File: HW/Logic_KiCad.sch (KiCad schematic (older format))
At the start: 11 parts, among them SW1 SW_SPDT, U1 ESP32-PICO-D4

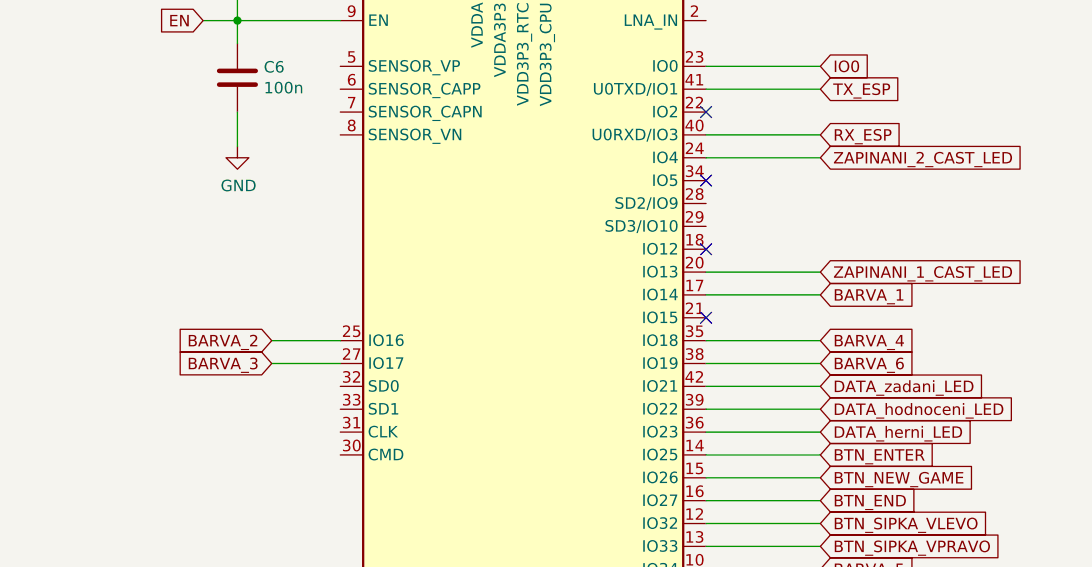
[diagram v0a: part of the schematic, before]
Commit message: repair mistake with tranzistors, repair programming ESP PICO
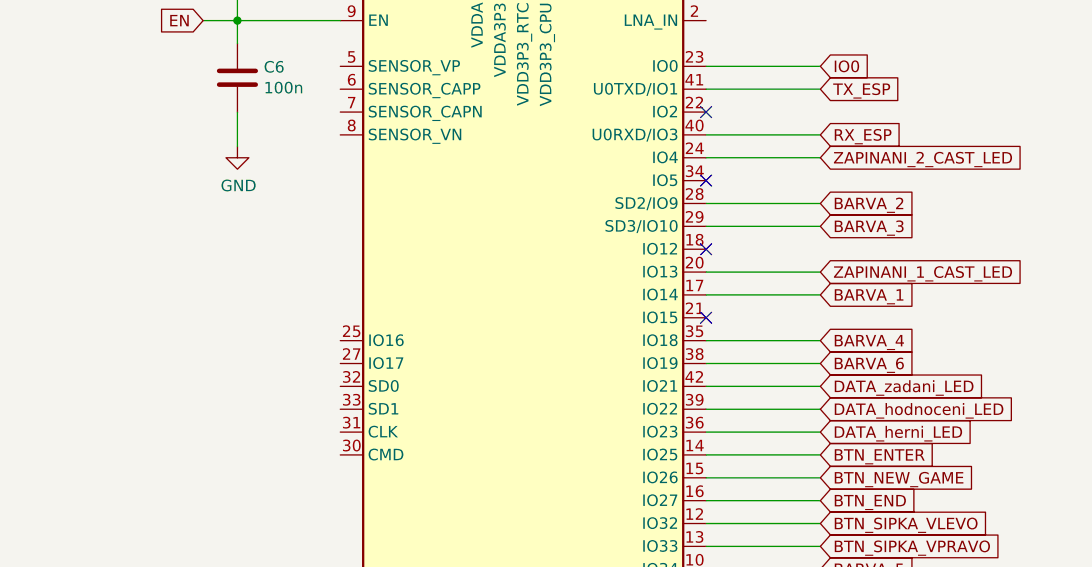
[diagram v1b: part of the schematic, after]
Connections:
- net BARVA_2: now also U1.28 (SD2/IO9); no longer U1.25 (IO16)
- net BARVA_3: now also U1.29 (SD3/IO10); no longer U1.27 (IO17)
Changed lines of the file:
@@
 Text GLabel 5950 5450 2    50   Input ~ 0
 BARVA_1
-Text GLabel 3550 5650 0    50   Input ~ 0
+Text GLabel 5950 5050 2    50   Input ~ 0
 BARVA_2
 Wire Wire Line
@@
 F6 "GPIO_2" I R 1600 7150 50
 $EndSheet
-Text GLabel 3550 5750 0    50   Input ~ 0
+Text GLabel 5950 5150 2    50   Input ~ 0
 BARVA_3
 Text GLabel 5950 5650 2    50   Input ~ 0
@@
 Text GLabel 5950 5750 2    50   Input ~ 0
 BARVA_6
-Wire Wire Line
-	3550 5650 3850 5650
-Wire Wire Line
-	3850 5750 3550 5750
 Text GLabel 9750 4450 0    50   Input ~ 0
 BARVA_5
@@
 Wire Wire Line
 	9750 4050 9950 4050
+Wire Wire Line
+	5950 5050 5450 5050
+Wire Wire Line
+	5450 5150 5950 5150
 $EndSCHEMATC

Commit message: deposit of DPS, start v1.0
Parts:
- added D?: green, LED_SMD:LED_0603_1608Metric, symbol Device:LED
- added H? (x4): MountingHole, symbol Mechanical:MountingHole
- added R? (x2): 10k, Resistor_SMD:R_0402_1005Metric, symbol Device:R
- C6: value 100n -> 1u; LCSC C1525 -> (none)
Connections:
- net +3V3: now also D?.2 (A), R?.2
- net BARVA_5: now also R?.1
- net GND: now also R?.1
- net V_BAT_PRIME renamed +5V
- new net: D?.1 (K), R?.2
- no-connect marks 6 -> 17
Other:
- moved on the sheet: SW1

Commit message: start place components
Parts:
- added R4: 10k, Resistor_SMD:R_0402_1005Metric, symbol Device:R
- H1, H2, H3, H4: renamed from H?; footprint (none) -> MountingHole:MountingHole_3.2mm_M3_DIN965_Pad; LCSC (none) -> -
- gave numbers to parts that had none: 3
- renumbered C6 to C1, C4 to C3, C1 to C4, C3 to C5, C5 to C6, R2 to R1, R1 to R2
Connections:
- net MERENI_BATERKY is gone; now on net BARVA_4: U1.11 (IO35)
- net V_BAT_SPINANE is gone; now on net +5V: SW1.1 (A)
- net +3V3: now also R4.2
- net +5V: no longer SW1.2 (B)
- net BARVA_4: now also R4.1; no longer U1.35 (IO18)
- net ZAPINANI_3_CAST_LED: now also U1.35 (IO18)
- new net V_IN: SW1.2 (B)
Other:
- moved on the sheet: H1, H2, H3, H4

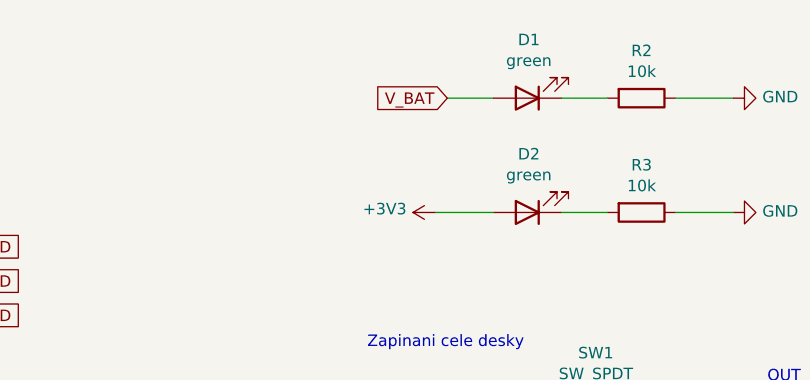
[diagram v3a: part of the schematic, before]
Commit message: change footprint of buttons, continue placing components, repair mistake in power voltage
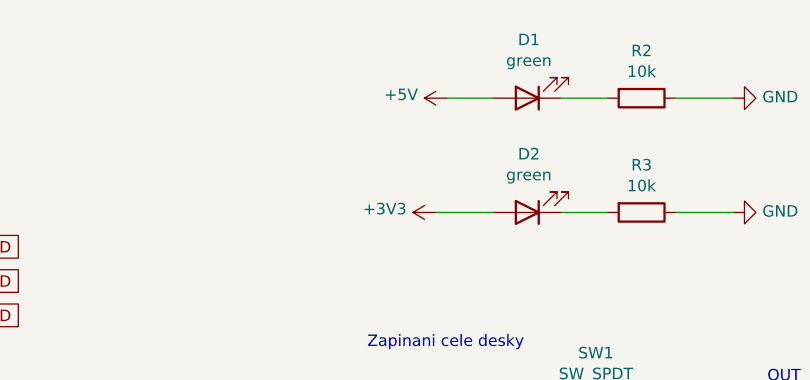
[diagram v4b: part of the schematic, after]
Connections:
- net V_BAT is gone; now on net +5V: D1.2 (A)
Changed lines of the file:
@@
 	-1   0    0    1
 $EndComp
-Text GLabel 4600 900  0    50   Input ~ 0
-V_BAT
 $Comp
 L Device:R R2
@@
 F5 "V_LED_3" I L 9950 1200 50
 $EndSheet
+$Comp
+L power:+5V #PWR?
+U 1 1 5FBE4E34
+P 4600 900
+F 0 "#PWR?" H 4600 750 50  0001 C CNN
+F 1 "+5V" V 4615 1028 50  0000 L CNN
+F 2 "" H 4600 900 50  0001 C CNN
+F 3 "" H 4600 900 50  0001 C CNN
+	1    4600 900
+	0    -1   -1   0
+$EndComp
 $EndSCHEMATC

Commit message: repair footprint of P and N MOS, add order codes for JLCPCB, preparing for fab
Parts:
- C1: JLCPCB_CORRECTION (none) -> 0;0;0; LCSC (none) -> C52923
- C2, C3, C4, C5, C6, D1, D2, H1, H2, H3, H4, R1, R2, R3, R4, R5, SW1: JLCPCB_CORRECTION (none) -> 0;0;0
- U1: JLCPCB_CORRECTION (none) -> 0;0;270
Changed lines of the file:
@@
 F 3 "https://www.espressif.com/sites/default/files/documentation/esp32-pico-d4_datasheet_en.pdf" H 4900 4650 50  0001 C CNN
 F 4 "C193707" H 4650 5650 50  0001 C CNN "LCSC"
+F 5 "0;0;270" H 4650 5650 50  0001 C CNN "JLCPCB_CORRECTION"
 	1    4650 5650
 	1    0    0    -1
@@
 F 3 "~" H 3400 3950 50  0001 C CNN
 F 4 "C25744" H 3400 3950 50  0001 C CNN "LCSC"
+F 5 "0;0;0" H 3400 3950 50  0001 C CNN "JLCPCB_CORRECTION"
 	1    3400 3950
 	1    0    0    -1
@@
 F 2 "Capacitor_SMD:C_0402_1005Metric" H 3438 4350 50  0001 C CNN
 F 3 "~" H 3400 4500 50  0001 C CNN
-F 4 "" H 3400 4500 50  0001 C CNN "LCSC"
+F 4 "C52923" H 3400 4500 50  0001 C CNN "LCSC"
+F 5 "0;0;0" H 3400 4500 50  0001 C CNN "JLCPCB_CORRECTION"
 	1    3400 4500
 	-1   0    0    1
@@
 F 3 "~" H 4950 3150 50  0001 C CNN
 F 4 "C15525" H 4950 3150 50  0001 C CNN "LCSC"
+F 5 "0;0;0" H 4950 3150 50  0001 C CNN "JLCPCB_CORRECTION"
 	1    4950 3150
 	0    1    1    0
@@
 F 3 "~" H 4950 4000 50  0001 C CNN
 F 4 "C1525" H 4950 4000 50  0001 C CNN "LCSC"
+F 5 "0;0;0" H 4950 4000 50  0001 C CNN "JLCPCB_CORRECTION"
 	1    4950 4000
 	0    1    1    0
@@
 F 3 "~" H 4950 900 50  0001 C CNN
 F 4 "C72043" H 4950 900 50  0001 C CNN "LCSC"
+F 5 "0;0;0" H 4950 900 50  0001 C CNN "JLCPCB_CORRECTION"
 	1    4950 900
 	-1   0    0    1
@@
 F 3 "~" H 5450 900 50  0001 C CNN
 F 4 "C25744" V 5450 900 50  0001 C CNN "LCSC"
+F 5 "0;0;0" H 5450 900 50  0001 C CNN "JLCPCB_CORRECTION"
 	1    5450 900
 	0    1    1    0
@@
 F 3 "~" H 5250 2300 50  0001 C CNN
 F 4 "ručně" H 5250 2300 50  0001 C CNN "LCSC"
+F 5 "0;0;0" H 5250 2300 50  0001 C CNN "JLCPCB_CORRECTION"
 	1    5250 2300
 	1    0    0    -1
@@
 F 3 "~" H 4250 4000 50  0001 C CNN
 F 4 "C1525" H 4250 4000 50  0001 C CNN "LCSC"
+F 5 "0;0;0" H 4250 4000 50  0001 C CNN "JLCPCB_CORRECTION"
 	1    4250 4000
 	0    1    1    0
@@
 F 3 "~" H 4250 3600 50  0001 C CNN
 F 4 "C1525" H 4250 3600 50  0001 C CNN "LCSC"
+F 5 "0;0;0" H 4250 3600 50  0001 C CNN "JLCPCB_CORRECTION"
 	1    4250 3600
 	0    1    1    0
@@
 F 3 "~" H 4950 3600 50  0001 C CNN
 F 4 "C1525" H 4950 3600 50  0001 C CNN "LCSC"
+F 5 "0;0;0" H 4950 3600 50  0001 C CNN "JLCPCB_CORRECTION"
 	1    4950 3600
 	0    1    1    0
@@
 F 3 "~" H 4950 1400 50  0001 C CNN
 F 4 "C72043" H 4950 1400 50  0001 C CNN "LCSC"
+F 5 "0;0;0" H 4950 1400 50  0001 C CNN "JLCPCB_CORRECTION"
 	1    4950 1400
 	-1   0    0    1
@@
 F 3 "~" H 5450 1400 50  0001 C CNN
 F 4 "C25744" V 5450 1400 50  0001 C CNN "LCSC"
+F 5 "0;0;0" H 5450 1400 50  0001 C CNN "JLCPCB_CORRECTION"
 	1    5450 1400
 	0    1    1    0
@@
 F 3 "~" H 700 7600 50  0001 C CNN
 F 4 "-" H 700 7600 50  0001 C CNN "LCSC"
+F 5 "0;0;0" H 700 7600 50  0001 C CNN "JLCPCB_CORRECTION"
 	1    700  7600
 	1    0    0    -1
@@
 F 3 "~" H 1550 7600 50  0001 C CNN
 F 4 "-" H 1550 7600 50  0001 C CNN "LCSC"
+F 5 "0;0;0" H 1550 7600 50  0001 C CNN "JLCPCB_CORRECTION"
 	1    1550 7600
 	1    0    0    -1
@@
 F 3 "~" H 1550 7300 50  0001 C CNN
 F 4 "-" H 1550 7300 50  0001 C CNN "LCSC"
+F 5 "0;0;0" H 1550 7300 50  0001 C CNN "JLCPCB_CORRECTION"
 	1    1550 7300
 	1    0    0    -1
@@
 F 3 "~" H 700 7300 50  0001 C CNN
 F 4 "-" H 700 7300 50  0001 C CNN "LCSC"
+F 5 "0;0;0" H 700 7300 50  0001 C CNN "JLCPCB_CORRECTION"
 	1    700  7300
 	1    0    0    -1
@@
 F 3 "~" H 5800 7000 50  0001 C CNN
 F 4 "C25744" V 5800 7000 50  0001 C CNN "LCSC"
+F 5 "0;0;0" H 5800 7000 50  0001 C CNN "JLCPCB_CORRECTION"
 	1    5800 7000
 	1    0    0    -1
@@
 F 3 "~" H 5650 7100 50  0001 C CNN
 F 4 "C25744" V 5650 7100 50  0001 C CNN "LCSC"
+F 5 "0;0;0" H 5650 7100 50  0001 C CNN "JLCPCB_CORRECTION"
 	1    5650 7100
 	1    0    0    -1
@@
 $EndSheet
 $Comp
-L power:+5V #PWR?
+L power:+5V #PWR0217
 U 1 1 5FBE4E34
 P 4600 900
-F 0 "#PWR?" H 4600 750 50  0001 C CNN
+F 0 "#PWR0217" H 4600 750 50  0001 C CNN
 F 1 "+5V" V 4615 1028 50  0000 L CNN
 F 2 "" H 4600 900 50  0001 C CNN

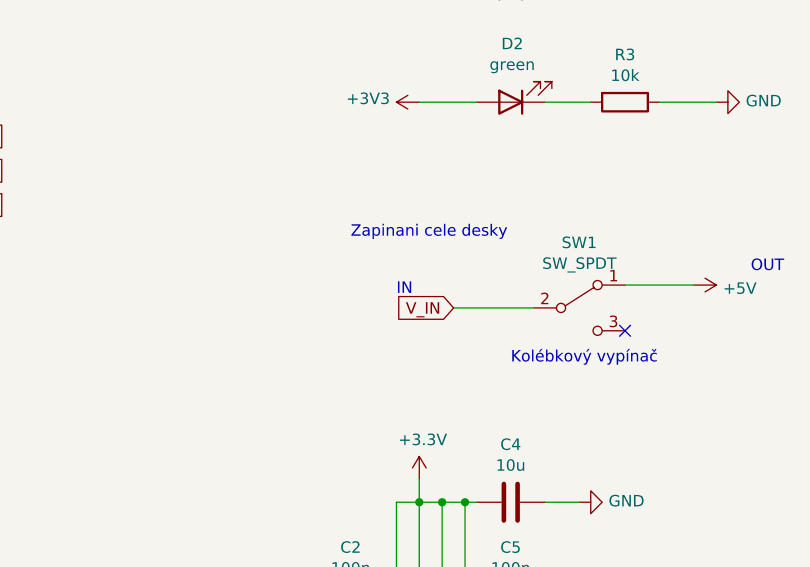
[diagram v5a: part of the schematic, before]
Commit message: V1.1 change SMD buttons, add diode on VCC
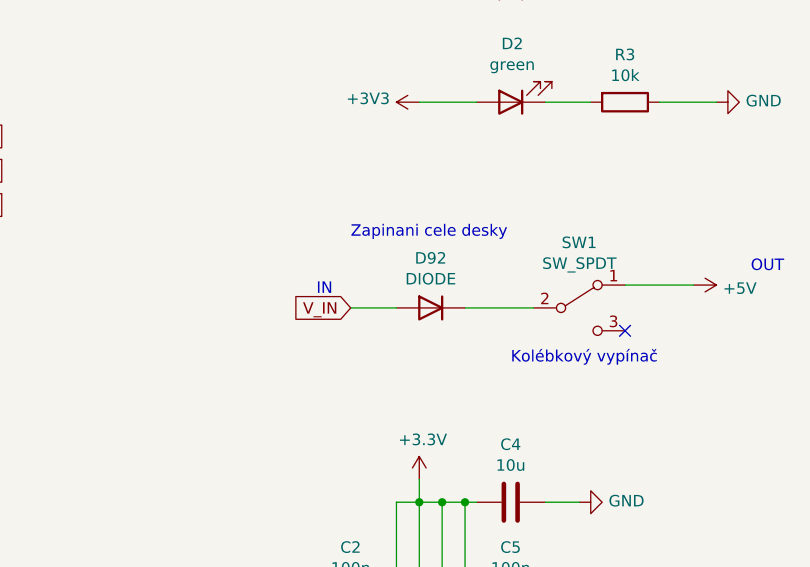
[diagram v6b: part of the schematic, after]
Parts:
- added D92: DIODE, Diode_SMD:D_SMA, symbol Simulation_SPICE:DIODE
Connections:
- net V_IN: now also D92.1 (A); no longer SW1.2 (B)
- new net: D92.2 (K), SW1.2 (B)
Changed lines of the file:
@@
 Wire Wire Line
 	5450 2200 5750 2200
-Wire Wire Line
-	5050 2300 4700 2300
 Text Notes 4250 2000 0    50   ~ 0
 Zapinani cele desky\n
 Text Notes 4950 2550 0    50   ~ 0
 Kolébkový vypínač
-Text Notes 4450 2250 0    50   ~ 0
+Text Notes 4100 2250 0    50   ~ 0
 IN\n
 Text Notes 6000 2150 0    50   ~ 0
@@
 Wire Wire Line
 	1600 4600 1450 4600
-Text GLabel 4700 2300 0    50   Input ~ 0
+Text GLabel 4250 2300 0    50   Input ~ 0
 V_IN
 $Comp
@@
 	0    -1   -1   0
 $EndComp
+$Comp
+L Simulation_SPICE:DIODE D92
+U 1 1 600E85D1
+P 4600 2300
+F 0 "D92" H 4600 2083 50  0000 C CNN
+F 1 "DIODE" H 4600 2174 50  0000 C CNN
+F 2 "Diode_SMD:D_SMA" H 4600 2300 50  0001 C CNN
+F 3 "~" H 4600 2300 50  0001 C CNN
+F 4 "Y" H 4600 2300 50  0001 L CNN "Spice_Netlist_Enabled"
+F 5 "D" H 4600 2300 50  0001 L CNN "Spice_Primitive"
+F 6 "C8678" H 4600 2300 50  0001 C CNN "LCSC"
+F 7 "0;0;180" H 4600 2300 50  0001 C CNN "JLCPCB_CORRECTION"
+	1    4600 2300
+	1    0    0    1
+$EndComp
+Wire Wire Line
+	4450 2300 4250 2300
+Wire Wire Line
+	4750 2300 5050 2300
 $EndSCHEMATC

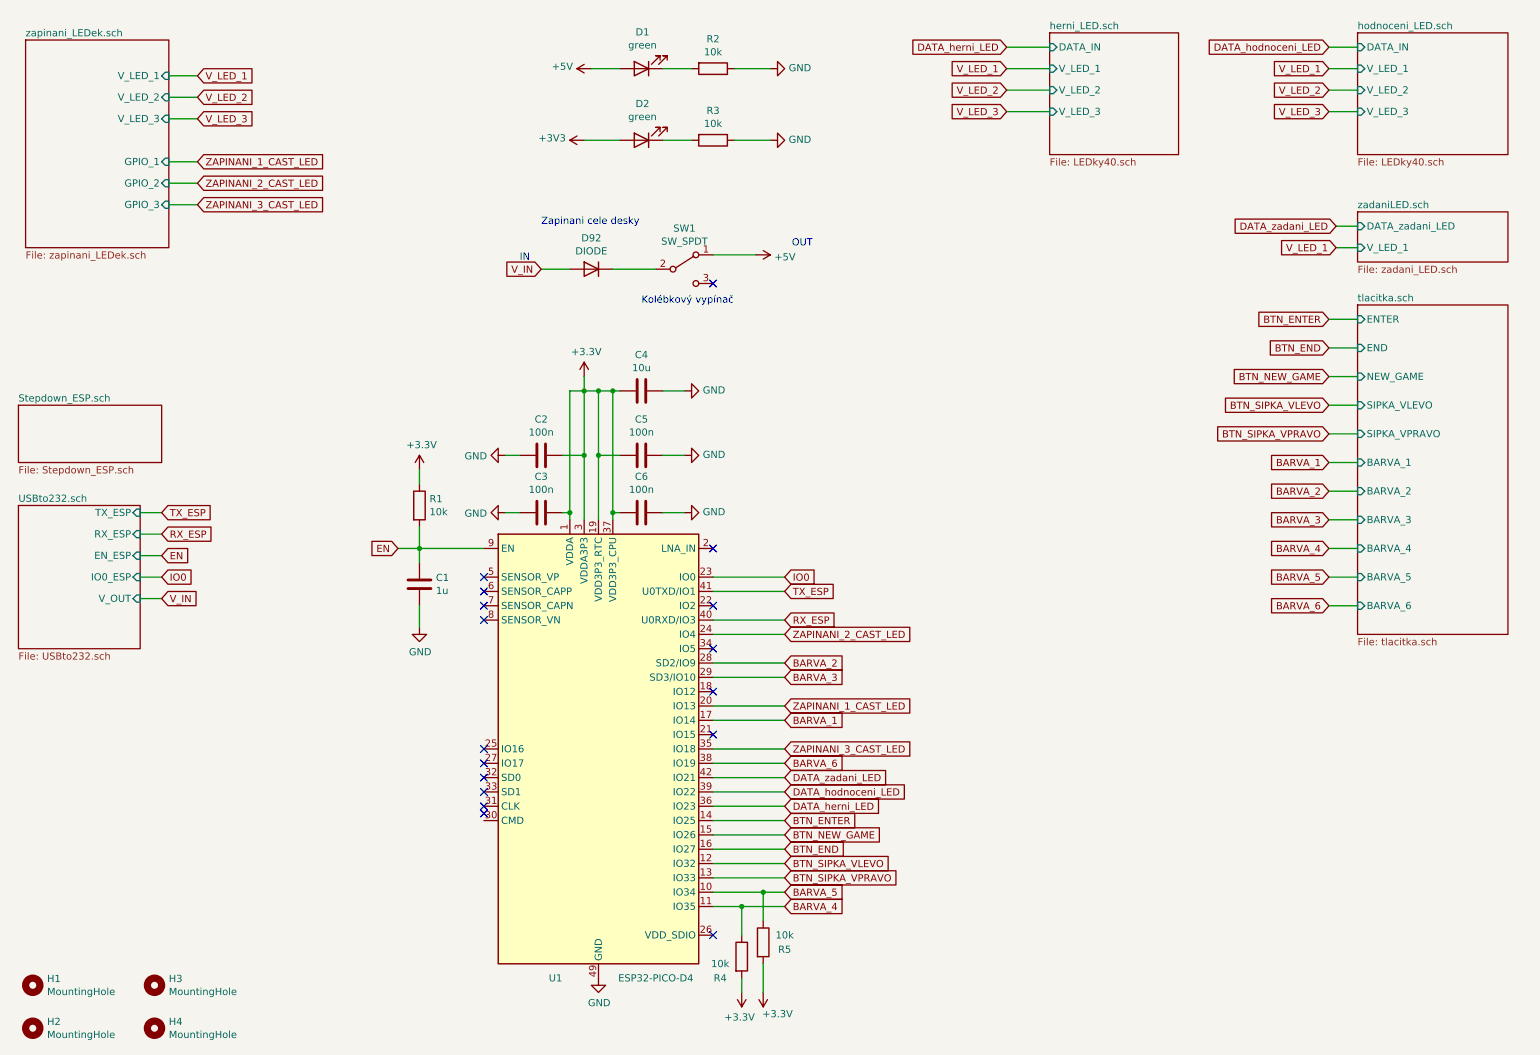
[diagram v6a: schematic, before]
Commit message: add level shifter
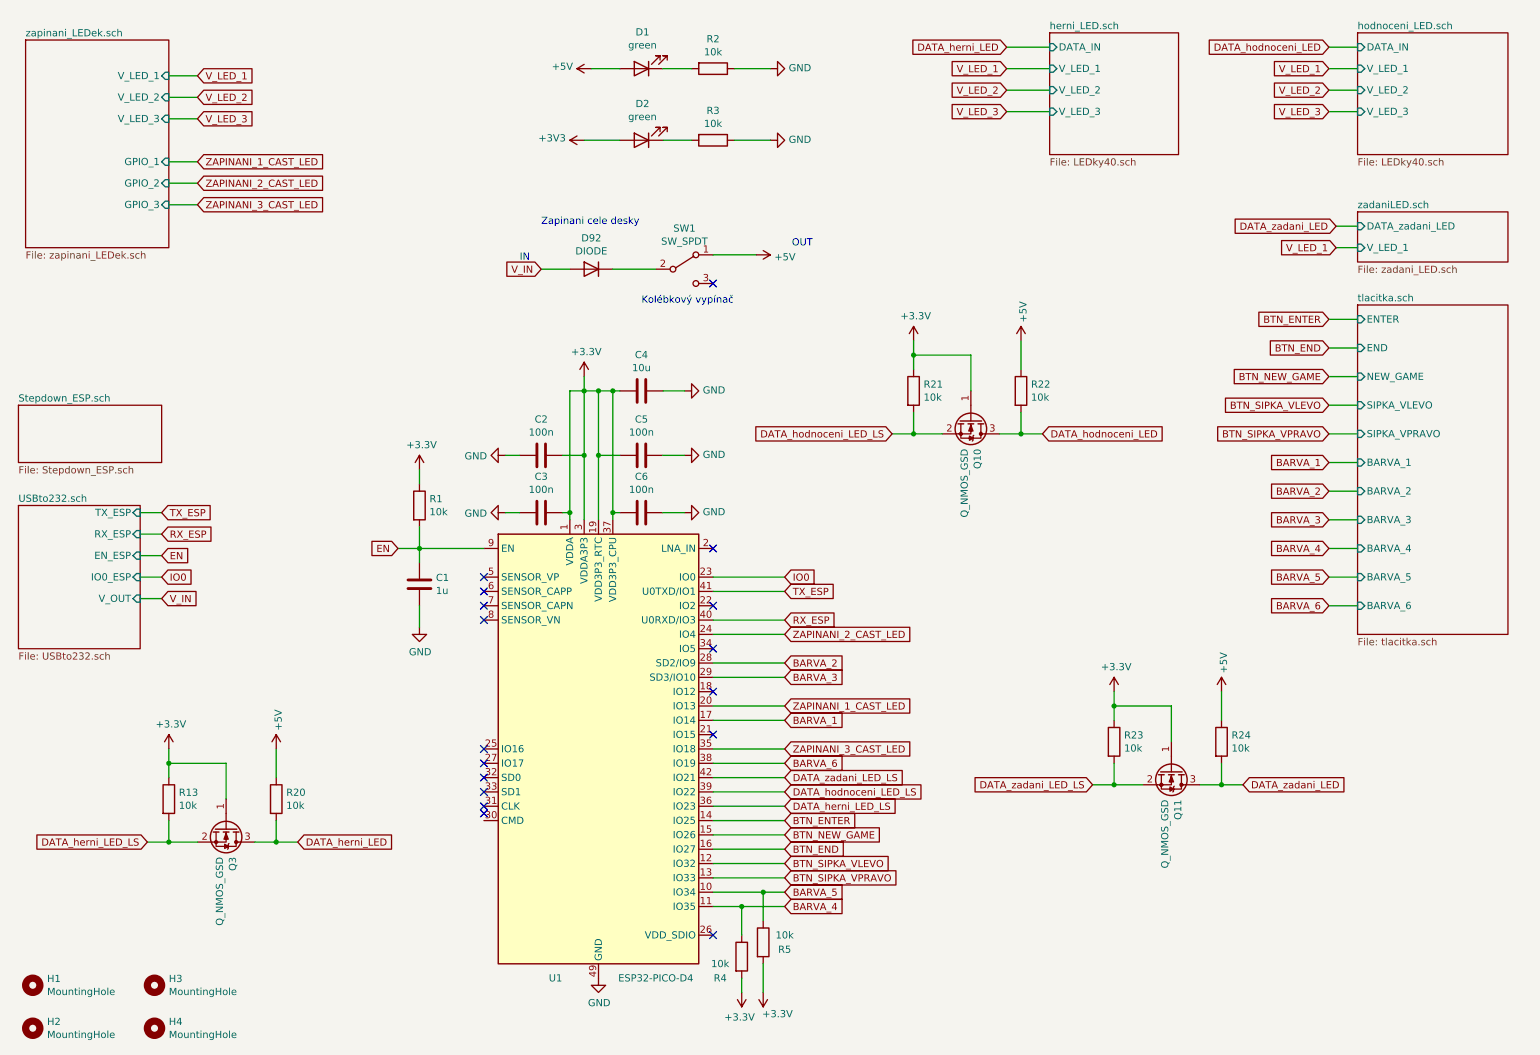
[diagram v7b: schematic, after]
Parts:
- added Q10, Q11, Q3: Q_NMOS_GSD, Package_TO_SOT_SMD:SOT-23, symbol Device:Q_NMOS_GSD
- added R13, R20, R21, R22, R23, R24: 10k, Resistor_SMD:R_0402_1005Metric, symbol Device:R
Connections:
- net +3V3: now also Q10.1 (G), Q11.1 (G), Q3.1 (G), R13.1, R21.1, R23.1
- net +5V: now also R20.1, R22.1, R24.1
- net DATA_herni_LED: now also Q3.3 (D), R20.2; no longer U1.36 (IO23)
- net DATA_hodnoceni_LED: now also Q10.3 (D), R22.2; no longer U1.39 (IO22)
- net DATA_zadani_LED: now also Q11.3 (D), R24.2; no longer U1.42 (IO21)
- new net DATA_herni_LED_LS: Q3.2 (S), R13.2, U1.36 (IO23)
- new net DATA_hodnoceni_LED_LS: Q10.2 (S), R21.2, U1.39 (IO22)
- new net DATA_zadani_LED_LS: Q11.2 (S), R23.2, U1.42 (IO21)
